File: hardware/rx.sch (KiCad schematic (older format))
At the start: 19 parts, among them P1 SMA, U11 SKY65404, U9 TRF37A73

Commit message: Added MFNs to components.
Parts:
- C179: MFN (none) -> GRM155R71E103KA01D
- C180: MFN (none) -> UMK105CG101JVHF
- C42, C46: MFN (none) -> CL05C180GB5NCNC
- C44: MFN (none) -> GRM1555C1H100FA01D
- C48: MFN (none) -> C1005C0G1H0R5B050BA
- C49: MFN (none) -> CL05B104KO5NNNC
- FB7, FB8: value BLM18PG181SN1D -> BLM18PG181SH1D; footprint fmcw:C_0603b -> Inductor_SMD:L_0603_1608Metric; MFN (none) -> BLM18PG181SH1D
- L1: footprint fmcw:C_0402b -> Inductor_SMD:L_0402_1005Metric; MFN (none) -> LQW15AN9N9J80D
- L2: footprint fmcw:C_0402b -> Inductor_SMD:L_0402_1005Metric; MFN (none) -> MLG1005S0N6CT000
- P1: symbol fmcw-rescue:SMA-fmcw3-rescue -> Connector:Conn_Coaxial; MFN (none) -> CONSMA003.062
- R22: footprint fmcw:R_0402b -> Resistor_SMD:R_0402_1005Metric; MFN (none) -> ERJ-2RKF1000X
- U11: MFN (none) -> SKY65404-31
- U9: MFN (none) -> TRF37A73IDSGR
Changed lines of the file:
@@
 F 2 "fmcw:XFDFN-6" H 6750 3800 60  0001 C CNN
 F 3 "http://www.skyworksinc.com/uploads/documents/SKY65404_31_201512J.pdf" H 6750 3800 60  0001 C CNN
+F 4 "SKY65404-31" H 0   0   50  0001 C CNN "MFN"
 	1    6800 3800
 	1    0    0    -1
@@
 AR Path="/59396B97/593BC25F" Ref="#PWR0124"  Part="1"
 AR Path="/593D90BA/593BC25F" Ref="#PWR0139"  Part="1"
-F 0 "#PWR0124" H 6850 4100 50  0001 C CNN
+F 0 "#PWR0139" H 6850 4100 50  0001 C CNN
 F 1 "GND" H 6850 4200 50  0000 C CNN
 F 2 "" H 6850 4350 60  0000 C CNN
@@
 AR Path="/59396B97/593BC2B3" Ref="#PWR0125"  Part="1"
 AR Path="/593D90BA/593BC2B3" Ref="#PWR0140"  Part="1"
-F 0 "#PWR0125" H 8000 3950 50  0001 C CNN
+F 0 "#PWR0140" H 8000 3950 50  0001 C CNN
 F 1 "GND" H 8000 4050 50  0000 C CNN
 F 2 "" H 8000 4200 60  0000 C CNN
@@
 AR Path="/59396B97/593BC302" Ref="#PWR0126"  Part="1"
 AR Path="/593D90BA/593BC302" Ref="#PWR0141"  Part="1"
-F 0 "#PWR0126" H 5900 4100 50  0001 C CNN
+F 0 "#PWR0141" H 5900 4100 50  0001 C CNN
 F 1 "GND" H 5900 4200 50  0000 C CNN
 F 2 "" H 5900 4350 60  0000 C CNN
@@
 AR Path="/59396B97/593BC396" Ref="R22"  Part="1"
 AR Path="/593D90BA/593BC396" Ref="R23"  Part="1"
-F 0 "R22" V 5830 3650 50  0000 C CNN
-F 1 "100" V 5750 3650 50  0000 C CNN
-F 2 "fmcw:R_0402b" V 5680 3650 30  0001 C CNN
+F 0 "R22" V 5543 3650 50  0000 C CNN
+F 1 "100" V 5634 3650 50  0000 C CNN
+F 2 "Resistor_SMD:R_0402_1005Metric" V 5680 3650 30  0001 C CNN
 F 3 "" H 5750 3650 30  0000 C CNN
+F 4 "ERJ-2RKF1000X" H 0   0   50  0001 C CNN "MFN"
 	1    5750 3650
 	0    1    1    0
@@
 F 0 "L2" V 8100 3300 50  0000 C CNN
 F 1 "0.6n" V 8250 3300 50  0000 C CNN
-F 2 "fmcw:C_0402b" H 8150 3300 60  0001 C CNN
+F 2 "Inductor_SMD:L_0402_1005Metric" H 8150 3300 60  0001 C CNN
 F 3 "" H 8150 3300 60  0000 C CNN
+F 4 "MLG1005S0N6CT000" H 0   0   50  0001 C CNN "MFN"
 	1    8150 3300
 	0    -1   -1   0
@@
 F 2 "Capacitor_SMD:C_0402_1005Metric" H 8638 3300 30  0001 C CNN
 F 3 "" H 8600 3450 60  0000 C CNN
+F 4 "CL05B104KO5NNNC" H 0   0   50  0001 C CNN "MFN"
 	1    8600 3450
 	1    0    0    -1
@@
 AR Path="/59396B97/593BC7DB" Ref="#PWR0127"  Part="1"
 AR Path="/593D90BA/593BC7DB" Ref="#PWR0142"  Part="1"
-F 0 "#PWR0127" H 8600 3350 50  0001 C CNN
+F 0 "#PWR0142" H 8600 3350 50  0001 C CNN
 F 1 "GND" H 8600 3450 50  0000 C CNN
 F 2 "" H 8600 3600 60  0000 C CNN
@@
 	7600 3950 8450 3950
 $Comp
-L fmcw-rescue:SMA-fmcw3-rescue P1
+L Connector:Conn_Coaxial P1
 U 1 1 593BCCCA
 P 9150 3950
@@
 F 2 "fmcw:CONSMA003.062" H 9150 3950 60  0001 C CNN
 F 3 "" H 9150 3950 60  0000 C CNN
+F 4 "CONSMA003.062" H 9150 3950 50  0001 C CNN "MFN"
 	1    9150 3950
 	1    0    0    -1
@@
 L power:GND #PWR0128
 U 1 1 593BCD59
-P 9150 4100
+P 9150 4250
 AR Path="/59396B97/593BCD59" Ref="#PWR0128"  Part="1"
 AR Path="/593D90BA/593BCD59" Ref="#PWR0143"  Part="1"
-F 0 "#PWR0128" H 9150 3850 50  0001 C CNN
-F 1 "GND" H 9150 3950 50  0000 C CNN
-F 2 "" H 9150 4100 60  0000 C CNN
-F 3 "" H 9150 4100 60  0000 C CNN
-	1    9150 4100
+F 0 "#PWR0143" H 9150 4000 50  0001 C CNN
+F 1 "GND" H 9150 4100 50  0000 C CNN
+F 2 "" H 9150 4250 60  0000 C CNN
+F 3 "" H 9150 4250 60  0000 C CNN
+	1    9150 4250
 	1    0    0    -1
 $EndComp
@@
 F 2 "Capacitor_SMD:C_0402_1005Metric" H 8488 4050 30  0001 C CNN
 F 3 "" H 8450 4200 60  0000 C CNN
+F 4 "C1005C0G1H0R5B050BA" H 0   0   50  0001 C CNN "MFN"
 	1    8450 4200
 	1    0    0    -1
@@
 AR Path="/59396B97/593BCF37" Ref="#PWR0129"  Part="1"
 AR Path="/593D90BA/593BCF37" Ref="#PWR0144"  Part="1"
-F 0 "#PWR0129" H 8450 4100 50  0001 C CNN
+F 0 "#PWR0144" H 8450 4100 50  0001 C CNN
 F 1 "GND" H 8450 4200 50  0000 C CNN
 F 2 "" H 8450 4350 60  0000 C CNN
@@
 F 2 "Capacitor_SMD:C_0402_1005Metric" H 5588 3800 30  0001 C CNN
 F 3 "" H 5550 3950 60  0000 C CNN
+F 4 "CL05C180GB5NCNC" H 0   0   50  0001 C CNN "MFN"
 	1    5550 3950
 	0    1    1    0
@@
 AR Path="/59396B97/593BD727" Ref="#PWR0130"  Part="1"
 AR Path="/593D90BA/593BD727" Ref="#PWR0145"  Part="1"
-F 0 "#PWR0130" H 4350 4600 50  0001 C CNN
+F 0 "#PWR0145" H 4350 4600 50  0001 C CNN
 F 1 "GND" H 4350 4700 50  0000 C CNN
 F 2 "" H 4350 4850 60  0000 C CNN
@@
 F 0 "L1" H 3928 3704 50  0000 L CNN
 F 1 "LQW15AN9N9J80D" H 3928 3795 50  0000 L CNN
-F 2 "fmcw:C_0402b" H 3850 3750 60  0001 C CNN
+F 2 "Inductor_SMD:L_0402_1005Metric" H 3850 3750 60  0001 C CNN
 F 3 "https://www.mouser.com/datasheet/2/281/JELF243A-0100-1380931.pdf" H 3850 3750 60  0001 C CNN
+F 4 "LQW15AN9N9J80D" H 0   0   50  0001 C CNN "MFN"
 	1    3850 3750
 	-1   0    0    1
@@
 F 2 "Capacitor_SMD:C_0402_1005Metric" H 4088 3100 30  0001 C CNN
 F 3 "" H 4050 3250 60  0000 C CNN
+F 4 "GRM1555C1H100FA01D" H 0   0   50  0001 C CNN "MFN"
 	1    4050 3250
 	1    0    0    -1
@@
 AR Path="/59396B97/593BDABD" Ref="#PWR0131"  Part="1"
 AR Path="/593D90BA/593BDABD" Ref="#PWR0146"  Part="1"
-F 0 "#PWR0131" H 4050 3150 50  0001 C CNN
+F 0 "#PWR0146" H 4050 3150 50  0001 C CNN
 F 1 "GND" H 4050 3250 50  0000 C CNN
 F 2 "" H 4050 3400 60  0000 C CNN
@@
 F 2 "Capacitor_SMD:C_0402_1005Metric" H 3488 3900 30  0001 C CNN
 F 3 "" H 3450 4050 60  0000 C CNN
+F 4 "CL05C180GB5NCNC" H 0   0   50  0001 C CNN "MFN"
 	1    3450 4050
 	0    1    1    0
@@
 AR Path="/59396B97/59751767" Ref="FB5"  Part="1"
 F 0 "FB5" V 3250 2650 50  0000 C CNN
-F 1 "BLM18PG181SN1D" V 3150 2750 50  0000 C CNN
-F 2 "fmcw:C_0603b" H 3300 2750 60  0001 C CNN
+F 1 "BLM18PG181SH1D" V 3150 2750 50  0000 C CNN
+F 2 "Inductor_SMD:L_0603_1608Metric" H 3300 2750 60  0001 C CNN
 F 3 "" H 3300 2750 60  0000 C CNN
+F 4 "BLM18PG181SH1D" H 0   0   50  0001 C CNN "MFN"
 	1    3300 2750
 	0    1    1    0
@@
 AR Path="/593D90BA/59751D9B" Ref="#PWR0147"  Part="1"
 AR Path="/59396B97/59751D9B" Ref="#PWR0132"  Part="1"
-F 0 "#PWR0132" H 5000 2800 50  0001 C CNN
+F 0 "#PWR0147" H 5000 2800 50  0001 C CNN
 F 1 "GND" H 5000 2900 50  0000 C CNN
 F 2 "" H 5000 3050 60  0000 C CNN
@@
 AR Path="/593D90BA/59752325" Ref="#PWR0148"  Part="1"
 AR Path="/59396B97/59752325" Ref="#PWR0133"  Part="1"
-F 0 "#PWR0133" H 2900 2900 50  0001 C CNN
+F 0 "#PWR0148" H 2900 2900 50  0001 C CNN
 F 1 "GND" H 2900 3000 50  0000 C CNN
 F 2 "" H 2900 3150 60  0000 C CNN
@@
 AR Path="/59396B97/597527FA" Ref="FB6"  Part="1"
 F 0 "FB6" V 8100 2450 50  0000 C CNN
-F 1 "BLM18PG181SN1D" V 8000 2600 50  0000 C CNN
-F 2 "fmcw:C_0603b" H 8150 2600 60  0001 C CNN
+F 1 "BLM18PG181SH1D" V 8000 2600 50  0000 C CNN
+F 2 "Inductor_SMD:L_0603_1608Metric" H 8150 2600 60  0001 C CNN
 F 3 "" H 8150 2600 60  0000 C CNN
+F 4 "BLM18PG181SH1D" H 0   0   50  0001 C CNN "MFN"
 	1    8150 2600
 	0    1    1    0
@@
 AR Path="/59396B97/59752C49" Ref="#PWR0134"  Part="1"
 AR Path="/593D90BA/59752C49" Ref="#PWR0149"  Part="1"
-F 0 "#PWR0134" H 9100 2650 50  0001 C CNN
+F 0 "#PWR0149" H 9100 2650 50  0001 C CNN
 F 1 "GND" H 9100 2750 50  0000 C CNN
 F 2 "" H 9100 2900 60  0000 C CNN
@@
 AR Path="/59396B97/59752CE4" Ref="#PWR0135"  Part="1"
 AR Path="/593D90BA/59752CE4" Ref="#PWR0150"  Part="1"
-F 0 "#PWR0135" H 7550 2700 50  0001 C CNN
+F 0 "#PWR0150" H 7550 2700 50  0001 C CNN
 F 1 "GND" H 7550 2800 50  0000 C CNN
 F 2 "" H 7550 2950 60  0000 C CNN
@@
 F 2 "fmcw:DFN-8-1EP_2x2mm_Pitch0.5mm" H 4350 4050 60  0001 C CNN
 F 3 "" H 4350 4050 60  0000 C CNN
+F 4 "TRF37A73IDSGR" H 0   0   50  0001 C CNN "MFN"
 	1    4550 4100
 	-1   0    0    -1
@@
 F 2 "Capacitor_SMD:C_0402_1005Metric" H 4738 2950 30  0001 C CNN
 F 3 "" H 4700 3100 60  0000 C CNN
+F 4 "UMK105CG101JVHF" H 0   0   50  0001 C CNN "MFN"
 	1    4700 3100
 	1    0    0    -1
@@
 AR Path="/59396B97/59761E7D" Ref="#PWR0136"  Part="1"
 AR Path="/593D90BA/59761E7D" Ref="#PWR0151"  Part="1"
-F 0 "#PWR0136" H 4700 3000 50  0001 C CNN
+F 0 "#PWR0151" H 4700 3000 50  0001 C CNN
 F 1 "GND" H 4700 3100 50  0000 C CNN
 F 2 "" H 4700 3250 60  0000 C CNN
@@
 F 2 "Capacitor_SMD:C_0402_1005Metric" H 4338 3100 30  0001 C CNN
 F 3 "" H 4300 3250 60  0000 C CNN
+F 4 "GRM155R71E103KA01D" H 0   0   50  0001 C CNN "MFN"
 	1    4300 3250
 	1    0    0    -1
@@
 AR Path="/59396B97/5976305E" Ref="#PWR0137"  Part="1"
 AR Path="/593D90BA/5976305E" Ref="#PWR0152"  Part="1"
-F 0 "#PWR0137" H 4300 3150 50  0001 C CNN
+F 0 "#PWR0152" H 4300 3150 50  0001 C CNN
 F 1 "GND" H 4300 3250 50  0000 C CNN
 F 2 "" H 4300 3400 60  0000 C CNN
@@
 AR Path="/593D90BA/59765731" Ref="#PWR0153"  Part="1"
 AR Path="/59396B97/59765731" Ref="#PWR0138"  Part="1"
-F 0 "#PWR0138" H 5200 4000 50  0001 C CNN
+F 0 "#PWR0153" H 5200 4000 50  0001 C CNN
 F 1 "GND" H 5200 4100 50  0000 C CNN
 F 2 "" H 5200 4250 60  0000 C CNN
@@
 Wire Wire Line
 	8300 3300 8600 3300
+Wire Wire Line
+	9150 4250 9150 4150
 $EndSCHEMATC

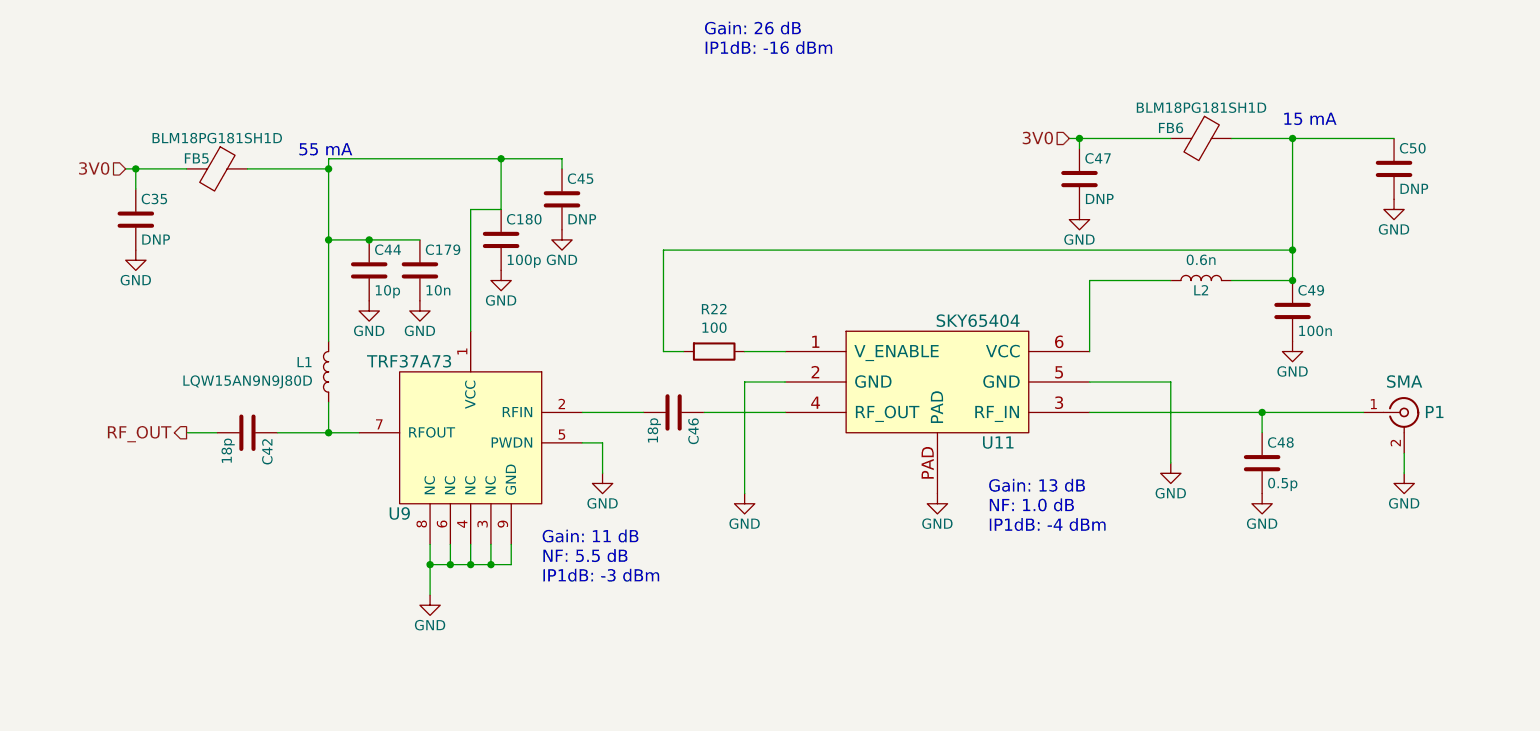
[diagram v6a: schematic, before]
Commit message: Fixed ERC errors.
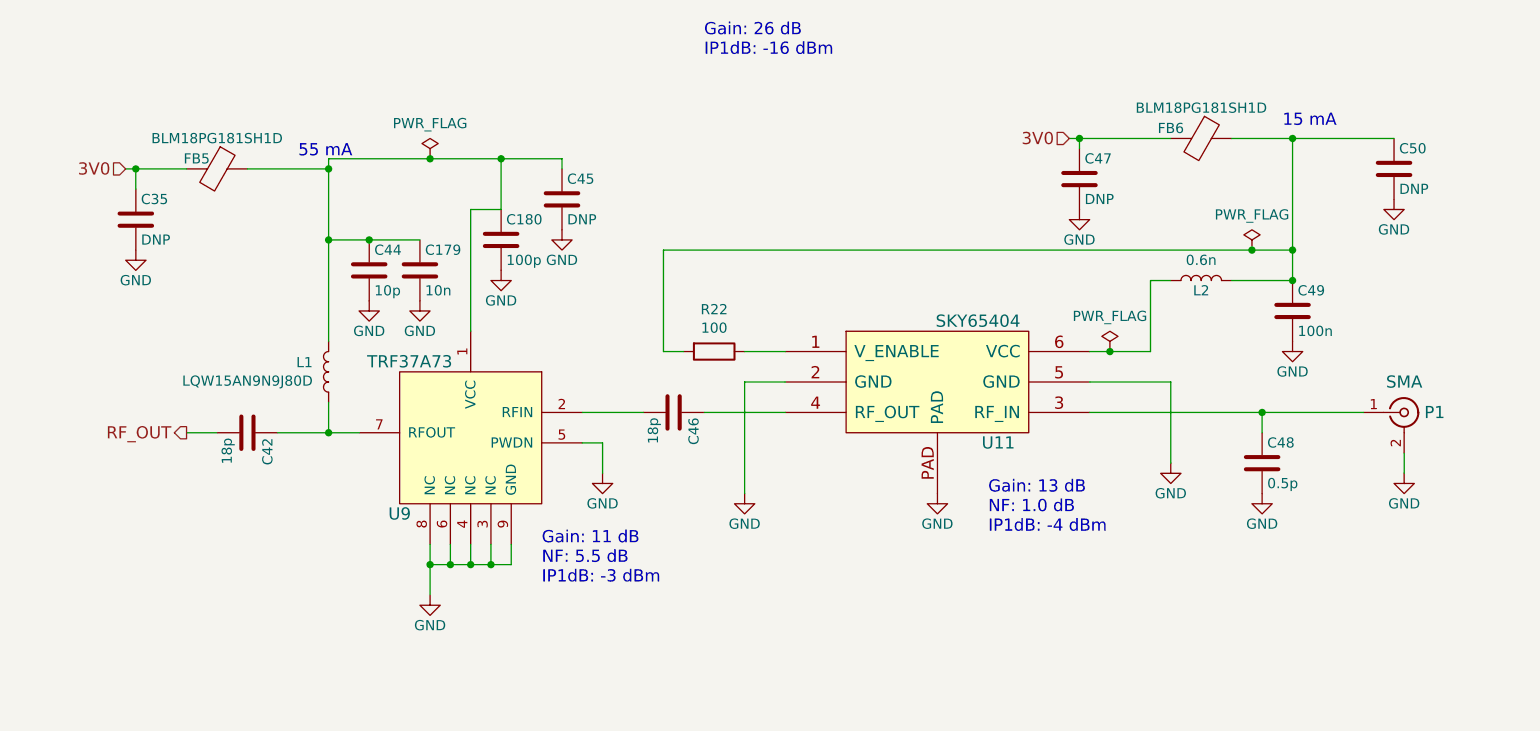
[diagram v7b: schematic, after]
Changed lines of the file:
@@
 Wire Wire Line
 	5600 3650 5500 3650
-Wire Wire Line
-	7600 3650 7600 3300
 $Comp
 L Device:L L2
@@
 	5500 3650 5500 3150
 Wire Wire Line
-	5500 3150 8600 3150
+	5500 3150 8400 3150
 Connection ~ 8600 3150
 Text Notes 7100 4550 0    60   ~ 0
@@
 	4350 4700 4350 4850
 Wire Wire Line
-	4700 2700 3850 2700
+	4700 2700 4350 2700
 Wire Wire Line
 	4050 3100 4300 3100
@@
 	3850 4050 4000 4050
 Wire Wire Line
-	7600 3300 8000 3300
-Wire Wire Line
 	8300 3300 8600 3300
 Wire Wire Line
 	9150 4250 9150 4150
+$Comp
+L power:PWR_FLAG #FLG0111
+U 1 1 5CF2FC64
+P 4350 2700
+AR Path="/59396B97/5CF2FC64" Ref="#FLG0111"  Part="1"
+AR Path="/593D90BA/5CF2FC64" Ref="#FLG0113"  Part="1"
+F 0 "#FLG0113" H 4350 2775 50  0001 C CNN
+F 1 "PWR_FLAG" H 4350 2874 50  0000 C CNN
+F 2 "" H 4350 2700 50  0001 C CNN
+F 3 "~" H 4350 2700 50  0001 C CNN
+	1    4350 2700
+	1    0    0    -1
+$EndComp
+Connection ~ 4350 2700
+Wire Wire Line
+	4350 2700 3850 2700
+$Comp
+L power:PWR_FLAG #FLG0112
+U 1 1 5CF2FCC1
+P 8400 3150
+AR Path="/59396B97/5CF2FCC1" Ref="#FLG0112"  Part="1"
+AR Path="/593D90BA/5CF2FCC1" Ref="#FLG0114"  Part="1"
+F 0 "#FLG0114" H 8400 3225 50  0001 C CNN
+F 1 "PWR_FLAG" H 8400 3324 50  0000 C CNN
+F 2 "" H 8400 3150 50  0001 C CNN
+F 3 "~" H 8400 3150 50  0001 C CNN
+	1    8400 3150
+	1    0    0    -1
+$EndComp
+Connection ~ 8400 3150
+Wire Wire Line
+	8400 3150 8600 3150
+Wire Wire Line
+	7600 3650 7700 3650
+Wire Wire Line
+	7900 3650 7900 3300
+Wire Wire Line
+	7900 3300 8000 3300
+$Comp
+L power:PWR_FLAG #FLG0102
+U 1 1 5CF3D956
+P 7700 3650
+AR Path="/59396B97/5CF3D956" Ref="#FLG0102"  Part="1"
+AR Path="/593D90BA/5CF3D956" Ref="#FLG0118"  Part="1"
+F 0 "#FLG0118" H 7700 3725 50  0001 C CNN
+F 1 "PWR_FLAG" H 7700 3824 50  0000 C CNN
+F 2 "" H 7700 3650 50  0001 C CNN
+F 3 "~" H 7700 3650 50  0001 C CNN
+	1    7700 3650
+	1    0    0    -1
+$EndComp
+Connection ~ 7700 3650
+Wire Wire Line
+	7700 3650 7900 3650
 $EndSCHEMATC
